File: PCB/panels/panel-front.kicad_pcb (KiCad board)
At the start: 2 copper layers, 140 x 35 mm, 4 parts

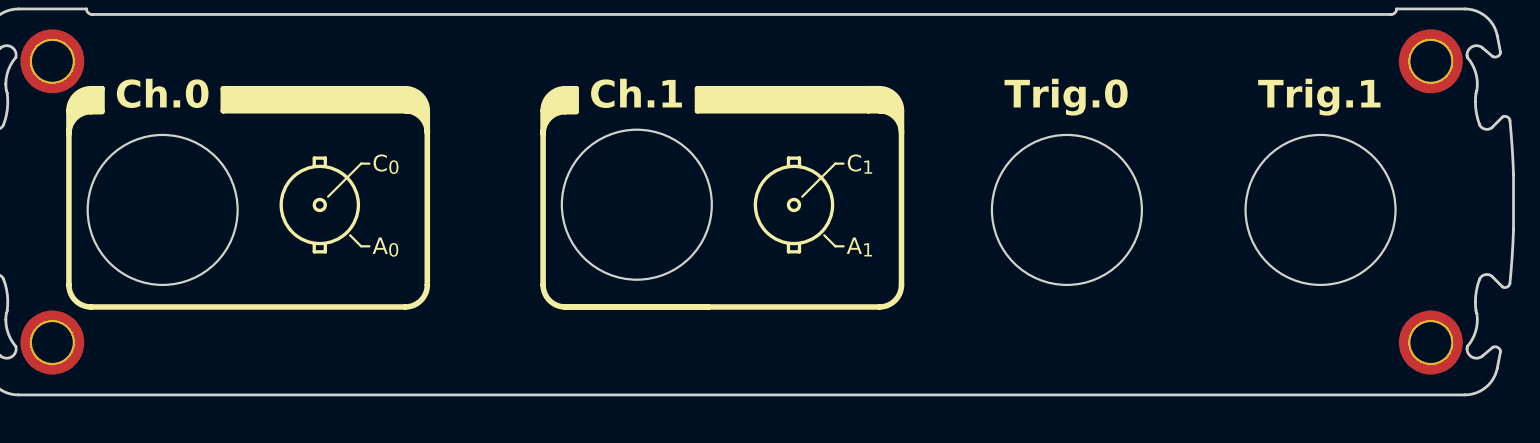
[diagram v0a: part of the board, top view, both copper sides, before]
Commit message: Add/edit silk screen and solder mask labels
Front panel:
- Add stimjim logo to solder mask
- Add "Dual isolated stimulus generator" to silk screen
Back panel:
- Shrink stimjim logo and center over usb cutout
- Add open ephys logo to solder mask
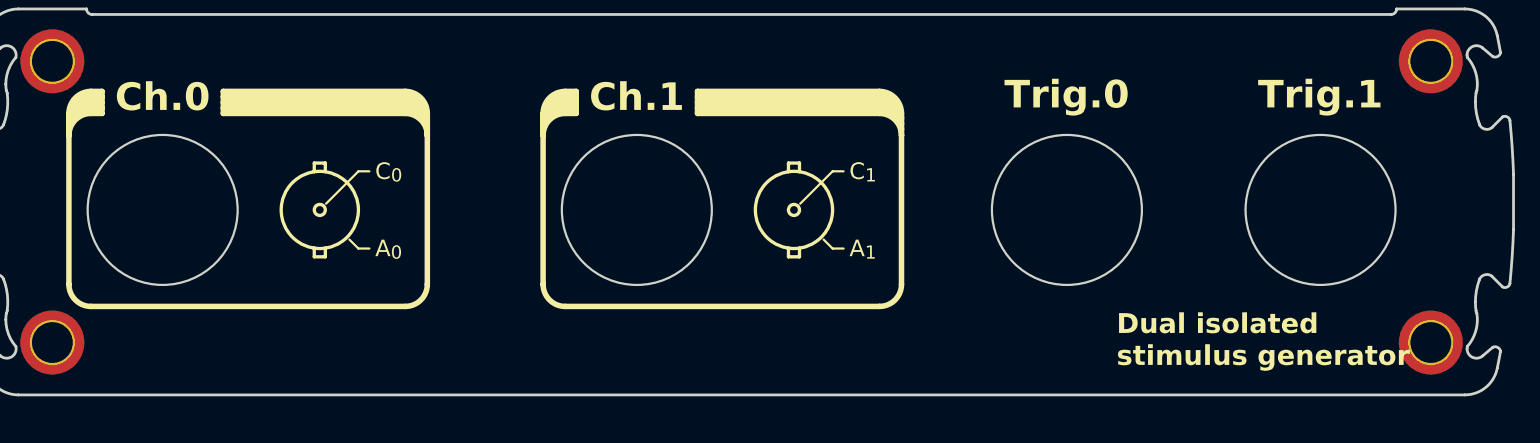
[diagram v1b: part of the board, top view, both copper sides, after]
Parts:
- added G***: LOGO, LOGO, F.Cu at (178.0, 114.5)
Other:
- outline, holes or cut-outs redrawn
- board text added: "Dual isolated stimulus generator"
